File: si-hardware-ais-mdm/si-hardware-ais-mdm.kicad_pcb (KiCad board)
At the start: 2 copper layers, 113.2 x 29 mm, 91 parts, among them J1 CN1, J2 CN2, J3 Conn_Coaxial, J4 USB_C_Receptacle_USB2.0_16P, Q1 IRLML6401, SW1 SW_Push, SW2 SW_Push, U1 LMR14206, U2 MCP73811T-420I-OT, U3 Si4362, U4 TA0395A, U5 Si4362, U6 ESP32-C6-MINI-1-H4, U7 LIS331HH, Y1 30MHz, Y2 30MHz

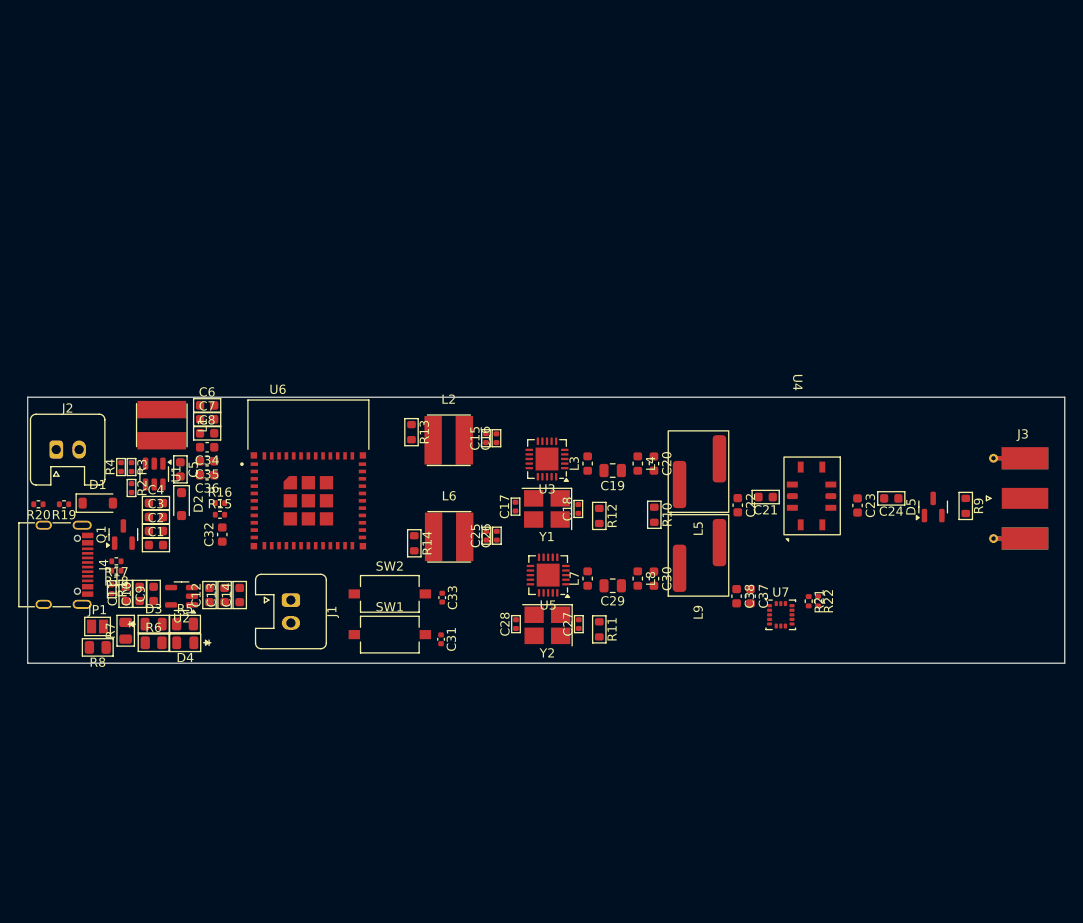
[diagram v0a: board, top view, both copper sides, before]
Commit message: scale board min length
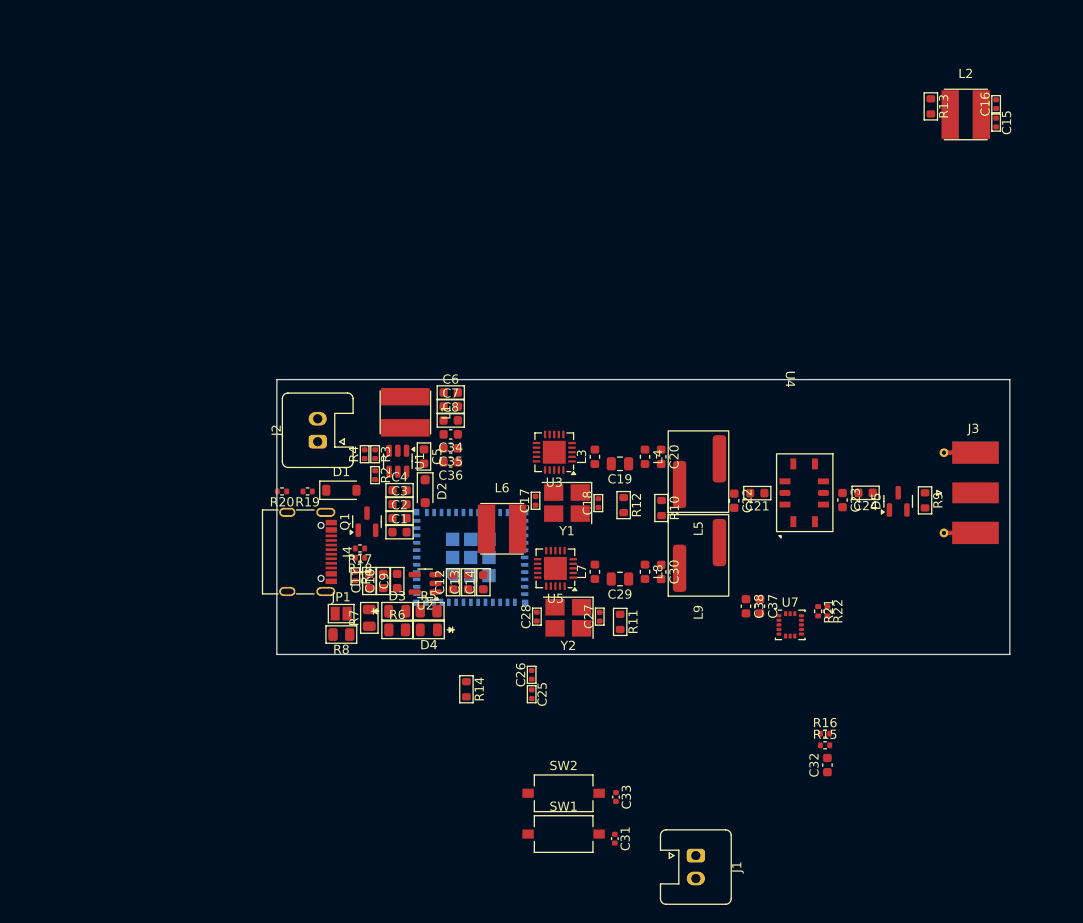
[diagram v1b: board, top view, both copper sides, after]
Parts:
- U6: moved to B.Cu
- moved C32 70.7 mm to (181.1, 125.4)
- moved R15 70.7 mm to (180.9, 123.2)
- moved R16 70.7 mm to (180.9, 121.9)
- moved R13 66.9 mm to (192.4, 53.5)
- moved L2 66.7 mm to (196.2, 54.4)
- moved C16 65.6 mm to (199.5, 53.2)
- moved C15 65.5 mm to (199.5, 55.2), turned to -90 degrees
- moved J1 52.3 mm to (166.8, 135.2)
- moved C33 28.9 mm to (158.0, 128.9)
- moved C31 28.9 mm to (157.9, 133.4)
- moved SW1 28.9 mm to (152.3, 132.9)
- moved SW2 28.9 mm to (152.3, 128.4)
- moved J2 28.6 mm to (125.5, 90.1), turned to 90 degrees
- moved C1 26.6 mm to (134.4, 99.9)
- moved C10 26.6 mm to (132.6, 105.3)
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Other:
- board size 113.2 x 29 mm -> 80 x 30 mm

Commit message: layout and routing
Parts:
- removed R14: 100K, CTS_Resistor_SMD:R_0603_1608Metric
- D1, R1, R19, R20: moved to B.Cu
- L2, L6: value 470uH 1A -> 59uH 1A; footprint CTS_Inductor_SMD:Inductor_4.7x4.7mm_H3.0mm -> Capacitor_SMD:C_0402_1005Metric
- L5, L9: value 60nH -> 62nH; footprint SI_Inductor:RF_Inductor -> Inductor_SMD:L_0603_1608Metric
- Y1, Y2: footprint Crystal:Crystal_SMD_3225-4Pin_3.2x2.5mm_HandSoldering -> Crystal:Crystal_SMD_SeikoEpson_TSX3225-4Pin_3.2x2.5mm
- moved C16 65.2 mm to (145.2, 89.2)
- moved C15 63.2 mm to (146.2, 89.2), turned to 90 degrees
- moved L2 63.1 mm to (144.7, 90.8)
- moved J1 48.4 mm to (125.5, 110.0), turned to 90 degrees
- moved C32 48.1 mm to (140.1, 100.3)
- moved R16 48.1 mm to (139.8, 96.9)
- moved R15 48.1 mm to (139.8, 98.2)
- moved C31 48.1 mm to (152.9, 85.6), turned to 90 degrees
- moved SW1 47.6 mm to (147.2, 85.6)
- moved SW2 43.5 mm to (159.6, 85.6), turned to 180 degrees
- moved C33 43.5 mm to (153.9, 85.6), turned to 90 degrees
- moved R13 40.2 mm to (169.0, 86.2)
- moved R12 18.0 mm to (142.9, 88.6), turned to 90 degrees
- moved C25 18.0 mm to (144.9, 100.1), turned to 180 degrees
- moved C26 16.9 mm to (144.9, 99.1), turned to 180 degrees
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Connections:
- U6 pad 19: unconnected-(U6-IO14-Pad19) -> /MCU/mdm.NSS1
- U6 pad 20: unconnected-(U6-IO15-Pad20) -> /MCU/mdm.IRQ1
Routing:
- net /MCU/mdm.RXDATA2: track 0.00 -> 33.6 mm, vias 0 -> 2
- net /MCU/mdm.RXCLK2: track 0.00 -> 33.2 mm, vias 0 -> 2
- net /MCU/mdm.GP2: track 0.00 -> 32.7 mm, vias 0 -> 2
- net /MCU/mdm.CTS2: track 0.00 -> 31.8 mm, vias 0 -> 2
- net /MCU/mdm.SDN2: track 0.00 -> 29.4 mm, vias 0 -> 3
- net /MCU/mdm.MISO: track 0.00 -> 28.4 mm, vias 0 -> 2
- net /MCU/mdm.SCLK: track 0.00 -> 27.2 mm, vias 0 -> 2
- net /MCU/mdm.NSS2: track 0.00 -> 24.4 mm, vias 0 -> 1
- net /MCU/mdm.MOSI: track 0.00 -> 23.8 mm, vias 0 -> 3
- net /MCU/mdm.IRQ2: track 0.00 -> 22.8 mm, vias 0 -> 1
- net /MCU/mdm.IRQ1: track 0.00 -> 20.9 mm, vias 0 -> 1
- net +3.3V: track 0.00 -> 19.9 mm
- net /MCU/mdm.RXDATA1: track 0.00 -> 19.8 mm, vias 0 -> 1
- net /MCU/mdm.RXCLK1: track 0.00 -> 17.5 mm, vias 0 -> 1
- net /MCU/mdm.GP1: track 0.00 -> 17.1 mm, vias 0 -> 1
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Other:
- board size 80 x 30 mm -> 78.2 x 30 mm
- copper layers 2 -> 4

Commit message: routing 2
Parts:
- moved U7 23.3 mm to (176.5, 88.2)
- moved C37 23.3 mm to (173.2, 86.2)
- moved C38 23.3 mm to (171.6, 86.2)
- moved R21 23.3 mm to (179.5, 86.7)
- moved R22 23.3 mm to (180.5, 86.7)
- moved R12 4.29 mm to (144.8, 92.5)
- moved C16 1.90 mm to (147.1, 89.1), turned to -90 degrees
- moved L2 1.74 mm to (145.0, 89.1), turned to 90 degrees
- moved R15 0.85 mm to (140.7, 98.1)
- moved C32 0.85 mm to (140.9, 100.3)
- moved R16 0.85 mm to (140.7, 96.9)
- moved C15 0.15 mm to (146.0, 89.1), turned to -90 degrees
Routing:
- net V_BATT: track 5.09 -> 41.4 mm
- net /MCU/mdm.SDN1: track 1.08 -> 19.5 mm, vias 1 -> 3
- net Net-(U6-IO13): track 0.00 -> 15.4 mm, vias 0 -> 1
- net /MCU/mdm.RXCLK1: track 17.5 -> 32.7 mm
- net /MCU/mdm.RXDATA1: track 19.8 -> 34.8 mm
- net Net-(U6-IO12): track 0.00 -> 14.7 mm, vias 0 -> 1
- net /MCU/mdm.NSS1: track 15.1 -> 28.8 mm
- net V_USB: track 5.09 -> 11.1 mm
- net D+: track 6.62 -> 10.3 mm
- net D-: track 6.38 -> 9.39 mm

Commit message: routing 3
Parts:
- added TP1: TestPoint, TestPoint:TestPoint_Pad_D1.0mm, F.Cu at (143.8, 101.7)
- added TP2: TestPoint, TestPoint:TestPoint_Pad_D1.0mm, F.Cu at (142.7, 96.4)
- C34, C35, C36: moved to B.Cu
- moved R13 25.1 mm to (145.8, 95.8), turned to 180 degrees
- moved C36 9.79 mm to (132.0, 86.7)
- moved C35 8.43 mm to (132.0, 88.3)
- moved C34 8.06 mm to (132.0, 89.8)
- moved R11 7.26 mm to (139.6, 100.7)
- moved C31 1.99 mm to (152.0, 87.4), turned to 0 degrees
- moved C33 1.99 mm to (154.8, 87.4), turned to 180 degrees
- moved R21 1.22 mm to (180.7, 86.7)
- moved R22 0.81 mm to (179.7, 86.7)
- moved C32 0.26 mm to (141.2, 100.3)
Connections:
- net Net-(U6-IO12) renamed i-
- net Net-(U6-IO13) renamed i+
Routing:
- net +3.3V: track 19.9 -> 108.0 mm, vias 0 -> 1
- net V_USB: track 11.1 -> 68.4 mm, vias 0 -> 4
- net SDA: track 0.00 -> 39.9 mm, vias 0 -> 2
- net SCL: track 0.00 -> 37.6 mm, vias 0 -> 2
- net V_BATT: track 41.4 -> 72.1 mm, vias 0 -> 1
- net Net-(C31-Pad1): track 0.00 -> 23.9 mm, vias 0 -> 2
- net Net-(U6-IO9): track 0.00 -> 22.5 mm, vias 0 -> 2
- net Net-(U6-EN): track 0.00 -> 13.6 mm, vias 0 -> 2
- net Net-(C15-Pad1): track 0.00 -> 9.83 mm
- net Net-(D1A-K): track 11.3 -> 20.1 mm, vias 0 -> 1
- net Net-(U7-SA0/SDO): track 0.00 -> 8.49 mm
- net Net-(U7-~{CS}): track 0.00 -> 5.95 mm
- net /MCU/mdm.MISO: track 28.4 -> 32.4 mm, vias 2 -> 4
- net /MCU/mdm.SDN2: track 29.4 -> 25.6 mm
- net Net-(J4-CC1): track 0.00 -> 3.12 mm, vias 0 -> 1
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- added copper zone on B.Cu, net GND
- added copper zone on F.Cu, net GND
- added copper zone on In1.Cu, net GND
- added copper zone on In2.Cu, net GND
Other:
- board text added: "+"
- board text added: "-"

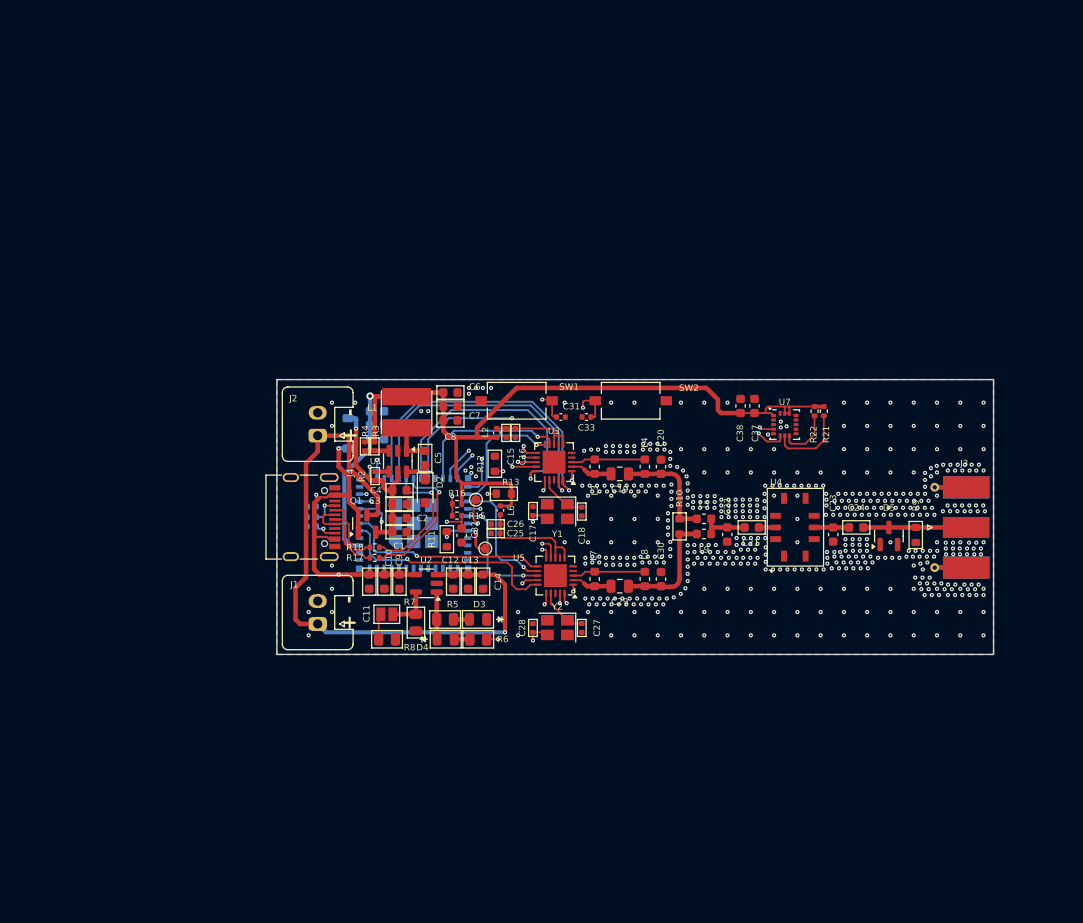
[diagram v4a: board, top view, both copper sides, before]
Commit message: added module flash
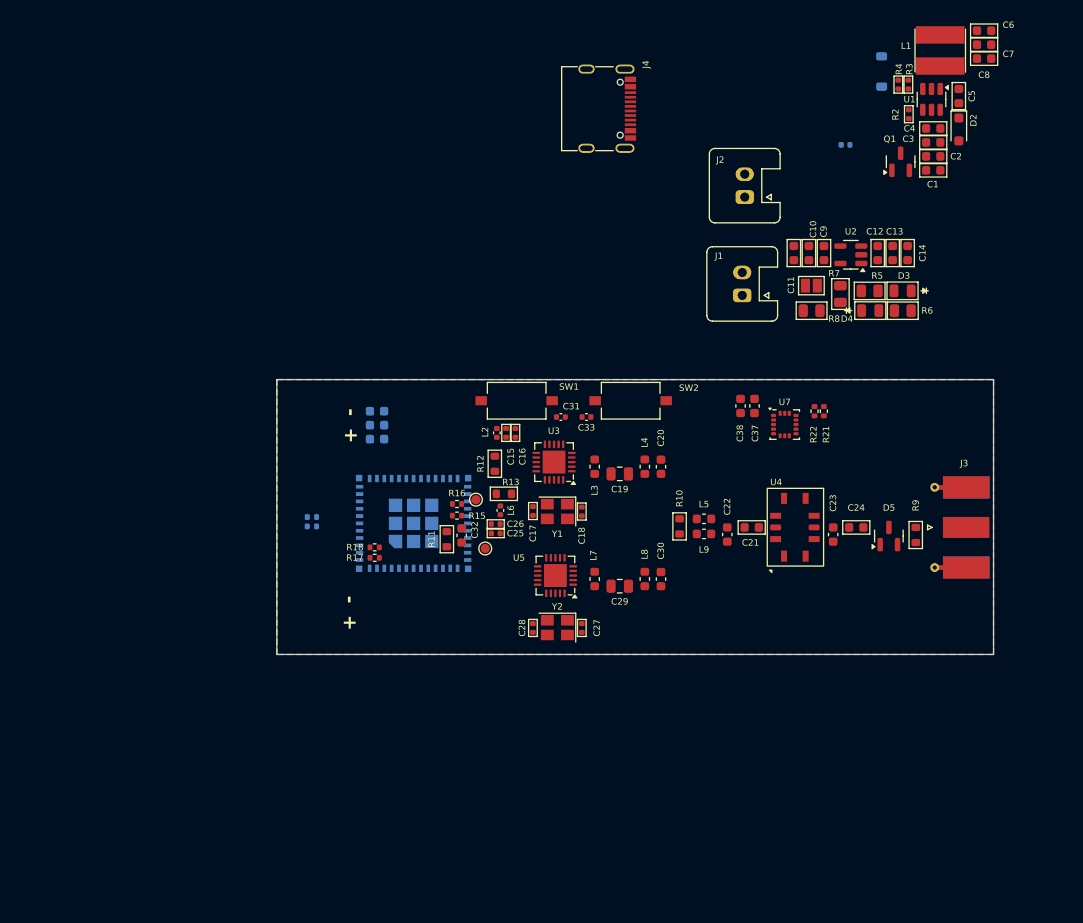
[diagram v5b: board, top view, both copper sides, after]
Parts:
- moved D1 70.4 mm to (187.0, 49.7)
- moved Q1 70.4 mm to (189.1, 59.5)
- moved R1 70.4 mm to (183.1, 57.7)
- moved C1 70.4 mm to (192.7, 60.5)
- moved C2 70.4 mm to (192.7, 58.9)
- moved C3 70.4 mm to (192.7, 57.4)
- moved C4 70.4 mm to (192.7, 55.9)
- moved C5 70.4 mm to (195.5, 52.3)
- moved C6 70.4 mm to (198.2, 45.2)
- moved C7 70.4 mm to (198.2, 46.7)
- moved C8 70.4 mm to (198.2, 48.3)
- moved D2 70.4 mm to (195.5, 56.0)
- moved L1 70.4 mm to (193.4, 47.4)
- moved R2 70.4 mm to (190.0, 54.3)
- moved R3 70.4 mm to (189.9, 51.1)
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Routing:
- net +3.3V: track 108.0 -> 0.00 mm, vias 1 -> 0
- net V_BATT: track 72.1 -> 0.00 mm, vias 1 -> 0
- net V_USB: track 68.4 -> 0.00 mm, vias 4 -> 0
- net SDA: track 39.9 -> 0.00 mm, vias 2 -> 0
- net SCL: track 37.6 -> 0.00 mm, vias 2 -> 0
- net /MCU/mdm.RXDATA1: track 34.8 -> 0.00 mm, vias 1 -> 0
- net /MCU/mdm.RXCLK2: track 34.0 -> 0.00 mm, vias 2 -> 0
- net /MCU/mdm.RXDATA2: track 33.6 -> 0.00 mm, vias 2 -> 0
- net /MCU/mdm.RXCLK1: track 33.0 -> 0.00 mm, vias 1 -> 0
- net /MCU/mdm.MISO: track 32.4 -> 0.00 mm, vias 4 -> 0
- net /MCU/mdm.GP2: track 30.8 -> 0.00 mm, vias 2 -> 0
- net /MCU/mdm.CTS2: track 29.6 -> 0.00 mm, vias 2 -> 0
- net /MCU/mdm.NSS1: track 28.3 -> 0.00 mm, vias 1 -> 0
- net /MCU/mdm.SCLK: track 27.2 -> 0.00 mm, vias 2 -> 0
- net /MCU/mdm.SDN2: track 25.6 -> 0.00 mm, vias 3 -> 0
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
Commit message: added chip flash 24LC64
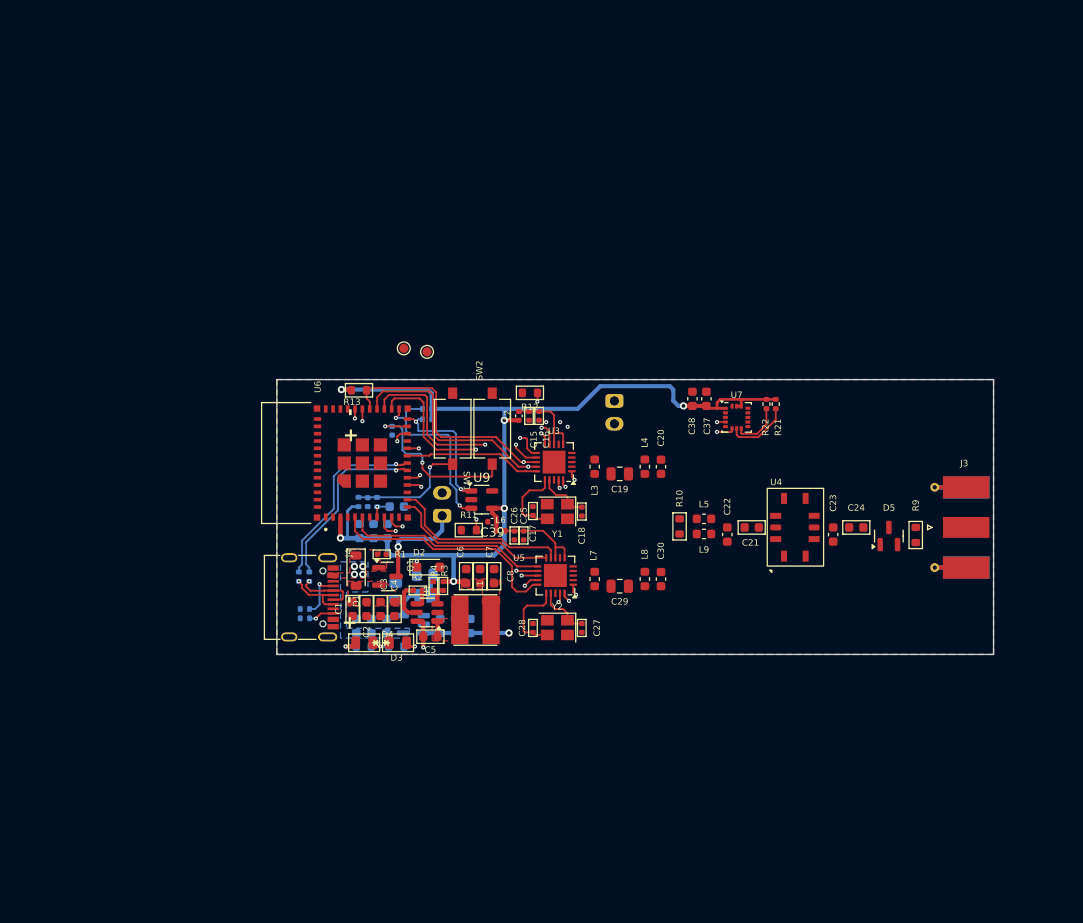
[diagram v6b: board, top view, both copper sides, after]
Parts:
- added C39: 104/10V, Capacitor_SMD:C_0402_1005Metric, F.Cu at (144.5, 98.8)
- added R14: 4.7K, Resistor_SMD:R_0402_1005Metric, B.Cu at (137.4, 86.5)
- added R23: 4.7K, Resistor_SMD:R_0402_1005Metric, B.Cu at (137.4, 87.6)
- added U9: 24AA02E-OT, Package_TO_SOT_SMD:SOT-23-5, F.Cu at (143.4, 96.4)
- C10, C11, C12, C13, C14, C31, C32, C33, C9, J1, J2, JP1, R15, R16, R17, R18, R7, R8, U2: moved to B.Cu
- D1, R1, U6: moved to F.Cu
- R5, R6: footprint CTS_Resistor_SMD:R_0805_2012Metric -> CTS_Resistor_SMD:R_0603_1608Metric; moved to B.Cu
- moved C5 82.5 mm to (137.8, 111.4), turned to 180 degrees
- moved C6 82.1 mm to (141.7, 104.7), turned to 90 degrees
- moved L1 80.2 mm to (142.7, 109.5), turned to 180 degrees
- moved C7 79.9 mm to (143.2, 104.7), turned to 90 degrees
- moved C1 79.4 mm to (129.3, 108.3), turned to -90 degrees
- moved C2 79.2 mm to (130.8, 108.3), turned to -90 degrees
- moved D1 79.1 mm to (129.7, 104.1), turned to -90 degrees
- moved C3 78.9 mm to (132.3, 108.3), turned to -90 degrees
- moved C4 78.8 mm to (133.9, 108.3), turned to -90 degrees
- moved U1 78.5 mm to (137.4, 108.7), turned to 180 degrees
- moved C8 77.8 mm to (144.7, 104.7), turned to 90 degrees
- moved D2 75.1 mm to (137.5, 103.8), turned to 0 degrees
- moved R2 74.7 mm to (136.4, 106.3), turned to 180 degrees
- moved R3 74.6 mm to (139.2, 105.8)
- moved R4 74.6 mm to (138.1, 105.8)
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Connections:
- net V_USB renamed V_BUS
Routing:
- net +3.3V: track 0.00 -> 109.9 mm, vias 0 -> 6
- net V_BATT: track 0.00 -> 64.3 mm, vias 0 -> 2
- net /MCU/mdm.SDN2: track 0.00 -> 42.5 mm, vias 0 -> 3
- net SDA: track 0.00 -> 41.2 mm, vias 0 -> 4
- net /MCU/mdm.MISO: track 0.00 -> 40.9 mm, vias 0 -> 2
- net /MCU/mdm.MOSI: track 0.00 -> 40.4 mm, vias 0 -> 2
- net /MCU/mdm.SCLK: track 0.00 -> 39.3 mm, vias 0 -> 3
- net SCL: track 0.00 -> 35.5 mm, vias 0 -> 5
- net /MCU/mdm.SDN1: track 0.00 -> 35.3 mm, vias 0 -> 3
- net /MCU/mdm.RXDATA2: track 0.00 -> 30.4 mm, vias 0 -> 2
- net /MCU/mdm.RXCLK2: track 0.00 -> 27.1 mm, vias 0 -> 2
- net /MCU/mdm.NSS2: track 0.00 -> 25.9 mm
- net /MCU/mdm.CTS1: track 0.00 -> 24.6 mm, vias 0 -> 2
- net /MCU/mdm.IRQ2: track 0.00 -> 22.2 mm
- net /MCU/mdm.GP1: track 0.00 -> 21.2 mm, vias 0 -> 2
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- added copper zone on F.Cu, net +3.3V
- added copper zone on F.Cu, net Net-(D1A-K)
- added copper zone on F.Cu, net Net-(U1-CB)
- added copper zone on B.Cu, net V_BUS
- added copper zone on F.Cu, net V_BUS
